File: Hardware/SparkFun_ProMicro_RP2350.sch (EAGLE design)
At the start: 61 parts, among them J2 QWIIC_RIGHT_ANGLE, J5 USB Female Type C Connector, U1 RT9080-33GJ5, U2 RP2350A, U3 WS2812_2020, U4 W25QXX128MBIT, Y1 12MHz

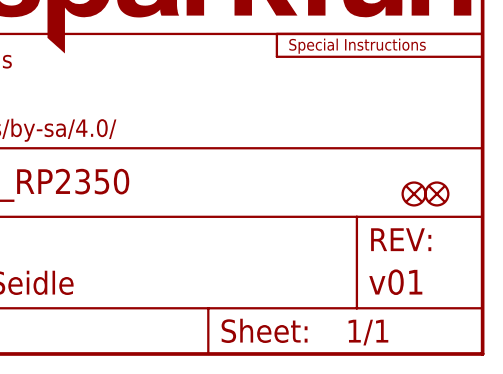
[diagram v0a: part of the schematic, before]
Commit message: v10 updates
Bump version number to v10
Move bottom pin silk labels away from pads
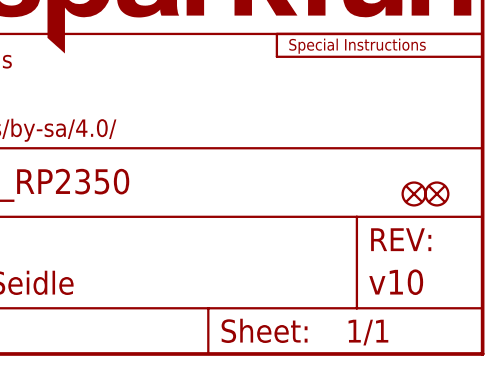
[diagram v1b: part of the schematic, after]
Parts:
- FRAME2: REV v01 -> v10
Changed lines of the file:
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@@
 <part name="FRAME2" library="SparkFun-Aesthetics" deviceset="FRAME-LEDGER" device="">
 <attribute name="DESIGNER" value="Dryw Wade"/>
-<attribute name="REV" value="v01"/>
+<attribute name="REV" value="v10"/>
 </part>
 <part name="TP3" library="SparkFun-Connectors" deviceset="TEST-POINT" device="3X5" value="TEST-POINT3X5"/>

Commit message: Add PSRAM
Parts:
- added C3: 0.1uF, SparkFun-Capacitors:0.1UF-0402T-6.3V-10%-X7R
- added JP3, JP4: FIDUCIAL1X2, SparkFun-Aesthetics:FIDUCIAL1X2
- added R4: 10k, SparkFun-Resistors:10KOHM-0402T-1/16W-1%
- added U5: APS6404L-3SQR-ZR, RP2350A:APS6404L-3SQR-ZR
- U1: device SparkFun-IC-Power:V_REG_RT9080 -> SparkFun-IC-Power:V_REG_RT9080-33GJ5
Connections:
- net QSPI-CS renamed FLASH_!CS!/BOOT
- new net PSRAM_!CS!: R4.1, U2.GPIO19, U5.!CE!
- net 3.3V: now also C3.1, R4.2, U5.VDD
- net GND: now also C3.2, U5.VSS
- net QSPI-0: now also U5.SI/SIO0
- net QSPI-1: now also U5.SO/SIO1
- net QSPI-2: now also U5.SIO2
- net QSPI-3: now also U5.SIO3
- net QSPI-CLK: now also U5.SCLK
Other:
- note added: "8MB PSRAM"
- moved on the sheet: U3

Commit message: Change version number to v09
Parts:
- FRAME2: REV v10 -> v09
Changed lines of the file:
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@@
 <part name="FRAME2" library="SparkFun-Aesthetics" deviceset="FRAME-LEDGER" device="">
 <attribute name="DESIGNER" value="Dryw Wade"/>
-<attribute name="REV" value="v10"/>
+<attribute name="REV" value="v09"/>
 </part>
 <part name="TP3" library="SparkFun-Connectors" deviceset="TEST-POINT" device="3X5" value="TEST-POINT3X5"/>

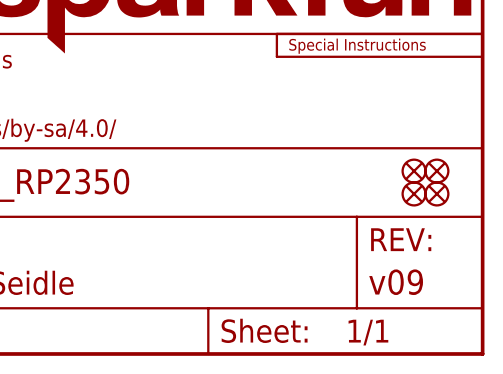
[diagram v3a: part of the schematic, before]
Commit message: Design review updates
Change version number to v02 instead of jumping to v09
Add PROD_ID to PSRAM
Nudge BOOT trace away from UART trace on adjacent layer
Fix "2" silk on bottom
Nudge C13 away from "6" silk on top
Fix acid trap on pad 5 of U1
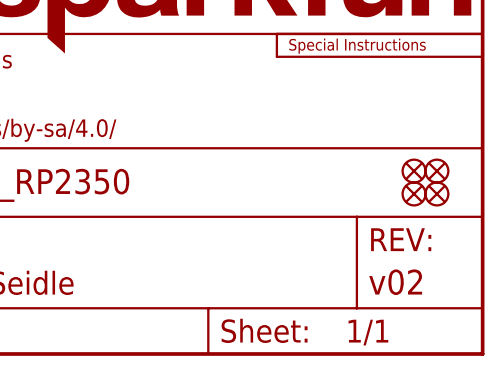
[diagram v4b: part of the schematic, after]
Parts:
- FRAME2: REV v09 -> v02
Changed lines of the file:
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@@
 <part name="FRAME2" library="SparkFun-Aesthetics" deviceset="FRAME-LEDGER" device="">
 <attribute name="DESIGNER" value="Dryw Wade"/>
-<attribute name="REV" value="v09"/>
+<attribute name="REV" value="v02"/>
 </part>
 <part name="TP3" library="SparkFun-Connectors" deviceset="TEST-POINT" device="3X5" value="TEST-POINT3X5"/>

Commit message: Bump version number to v10
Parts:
- FRAME2: REV v02 -> v10
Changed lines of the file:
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@@
 <part name="FRAME2" library="SparkFun-Aesthetics" deviceset="FRAME-LEDGER" device="">
 <attribute name="DESIGNER" value="Dryw Wade"/>
-<attribute name="REV" value="v02"/>
+<attribute name="REV" value="v10"/>
 </part>
 <part name="TP3" library="SparkFun-Connectors" deviceset="TEST-POINT" device="3X5" value="TEST-POINT3X5"/>
